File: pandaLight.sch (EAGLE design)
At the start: 158 parts, among them J1 PJ-037A, U1 MIC23451AAAYFL, U10 MT41J64M16, U11 PMOD-2X6, U12 PMOD-2X6, U13 PLR135-T10, U14 PLT133-T10W, U15 PLR135-T10, U16 TP10SQ, U17 TP10SQ, U18 PAN1322, U2 6SLX45CSG324, U3 TPD4S014SON, U4 FT2232HL, U5 93LC46BT-I/OT, U6 TPD12S016PWR, U7 TPD12S016PWR, U8 N25Q128AF8, U9 TPD12S016PWR, X1 USBUB-S, X2 HDMI_RECEPTICAL_A, X3 HDMI_RECEPTICAL_A, X4 HDMI_RECEPTICAL_A, Y1 403, Y2 20Mhz

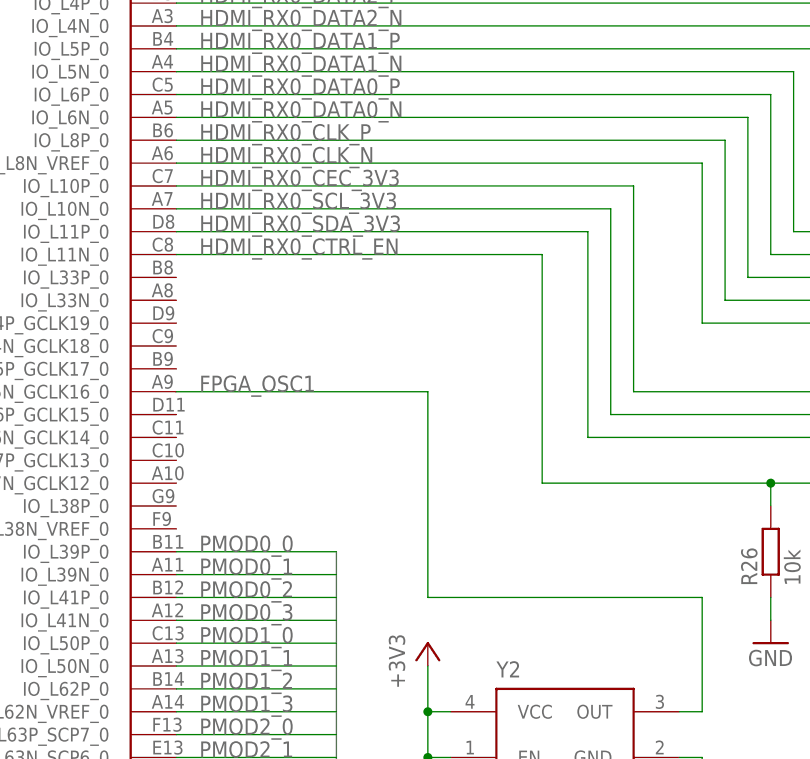
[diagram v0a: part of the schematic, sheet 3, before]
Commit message: Changed project name and file names to "pandaLight"; Routed connections FPGA to oscillator and HDMI_RX0
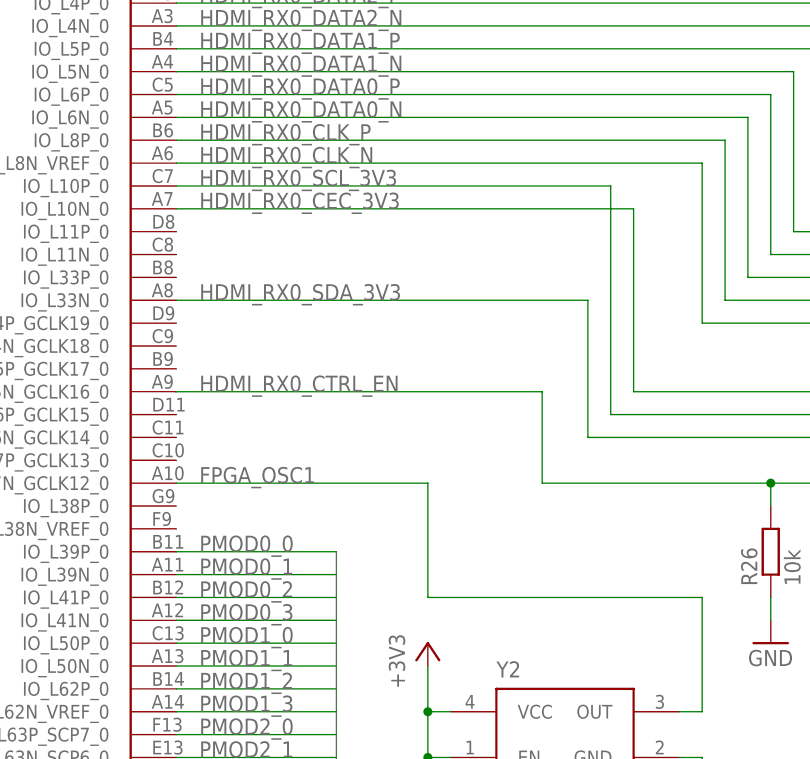
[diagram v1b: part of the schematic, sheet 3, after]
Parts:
- C1, C10, C2, C32, C6: device prj-hdmi:CAPACITOR1206 -> pandaLight:CAPACITOR1206
- C11, C12, C13, C14, C15, C16, C17, C18, C19, C20, C21, C22, C23, C24, C25, C26, C27, C28, C29, C3, C30, C31, C33, C34, C35, C36, C37, C38, C39, C4, C40, C41, C42, C43, C44, C45, C46, C47, C48, C49, C5, C50, C51, C52, C53, C54, C55, C56, C57, C58, C59, C60, C61, C62, C63, C64, C65, C66, C67, C68, C69, C7, C70, C8, C9: device prj-hdmi:CAPACITOR0402 -> pandaLight:CAPACITOR0402
- FB1, FB2: device prj-hdmi:FERRITE0402 -> pandaLight:FERRITE0402
- J1: device prj-hdmi:PJ-037A -> pandaLight:PJ-037A
- JP1, JP2, JP3: device prj-hdmi:JP2E -> pandaLight:JP2E
- L1, L2, L3: device prj-hdmi:INDUCTOR1008 -> pandaLight:INDUCTOR1008
- L4, L5: device prj-hdmi:INDUCTOR0603 -> pandaLight:INDUCTOR0603
- LED1, LED2: device prj-hdmi:LED0603 -> pandaLight:LED0603
- R1, R10, R11, R12, R13, R14, R15, R16, R17, R18, R19, R2, R20, R21, R22, R23, R24, R25, R26, R27, R28, R29, R3, R30, R31, R32, R33, R34, R35, R36, R37, R38, R39, R4, R40, R41, R42, R43, R44, R45, R46, R47, R5, R6, R7, R8, R9: device prj-hdmi:RESISTOR0402 -> pandaLight:RESISTOR0402
- RN1, RN2: device prj-hdmi:MNR18 -> pandaLight:MNR18
- SV1: device prj-hdmi:MA02-1 -> pandaLight:MA02-1
- SV2: device prj-hdmi:MA06-1 -> pandaLight:MA06-1
- U1: device prj-hdmi:MIC23451AAAYFL -> pandaLight:MIC23451AAAYFL
- U10: device prj-hdmi:MT41J64M16 -> pandaLight:MT41J64M16
- U11, U12: device prj-hdmi:PMOD-2X6 -> pandaLight:PMOD-2X6
- U13, U15: device prj-hdmi:PLR135-T10 -> pandaLight:PLR135-T10
- U14: device prj-hdmi:PLT133-T10W -> pandaLight:PLT133-T10W
- U16, U17: device prj-hdmi:TP10SQ -> pandaLight:TP10SQ
- U18: device prj-hdmi:PAN1322 -> pandaLight:PAN1322
- U2: device prj-hdmi:6SLX45CSG324 -> pandaLight:6SLX45CSG324
- U3: device prj-hdmi:TPD4S014SON -> pandaLight:TPD4S014SON
- U4: device prj-hdmi:FT2232HL -> pandaLight:FT2232HL
- U5: device prj-hdmi:93LC46BT-I/OT -> pandaLight:93LC46BT-I/OT
- U6, U7, U9: device prj-hdmi:TPD12S016PWR -> pandaLight:TPD12S016PWR
- U8: device prj-hdmi:N25Q128AF8 -> pandaLight:N25Q128AF8
- X1: device prj-hdmi:USBUB-S -> pandaLight:USBUB-S
- X2, X3, X4: device prj-hdmi:HDMI_RECEPTICAL_A -> pandaLight:HDMI_RECEPTICAL_A
- Y1: device prj-hdmi:403 -> pandaLight:403
- Y2: device prj-hdmi:636 -> pandaLight:636
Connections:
- net FPGA_OSC1: now also U2B0.IO_L37N_GCLK12_0; no longer U2B0.IO_L35N_GCLK16_0
- net HDMI_RX0_CEC_3V3: now also U2B0.IO_L10N_0; no longer U2B0.IO_L10P_0
- net HDMI_RX0_CTRL_EN: now also U2B0.IO_L35N_GCLK16_0; no longer U2B0.IO_L11N_0
- net HDMI_RX0_SCL_3V3: now also U2B0.IO_L10P_0; no longer U2B0.IO_L10N_0
- net HDMI_RX0_SDA_3V3: now also U2B0.IO_L33N_0; no longer U2B0.IO_L11P_0

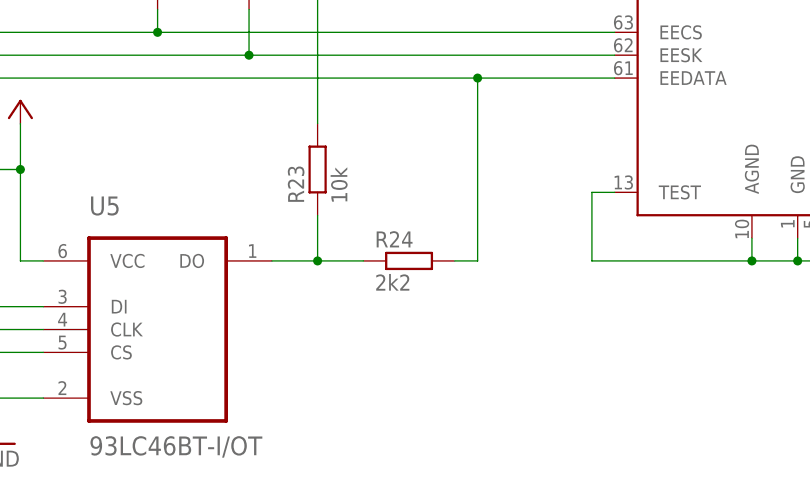
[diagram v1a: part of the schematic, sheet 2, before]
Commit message: Began adding BOM-ex parts
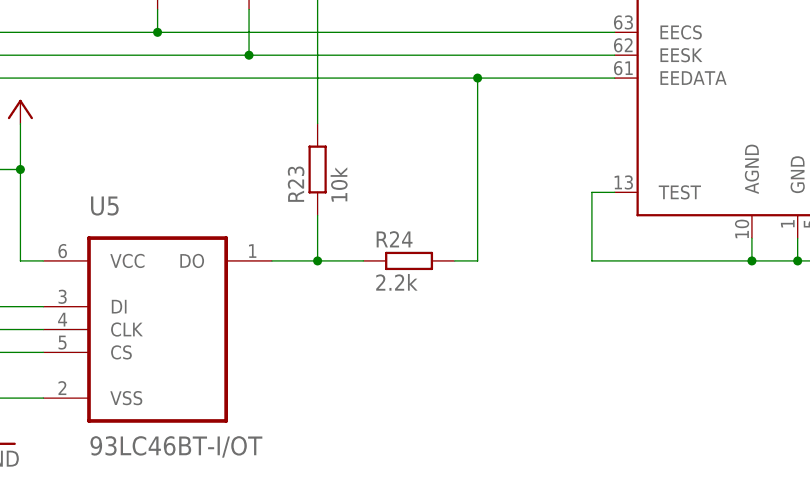
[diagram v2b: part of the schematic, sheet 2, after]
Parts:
- C1, C10, C2, C32, C6: PARTNO (none) -> CL31A107MQHNNNE
- C11, C15, C16, C17, C18, C23, C27, C29, C3, C31, C36, C43, C49, C55: PARTNO (none) -> C0603C475K9PACTU
- C12, C13, C14, C37, C38, C4, C44, C45, C5, C50, C51, C56, C57: PARTNO (none) -> C1005X5R0J474K050BB
- C19, C20, C21, C22, C24, C25, C26, C28, C30, C35, C39, C40, C41, C42, C46, C47, C48, C52, C53, C54, C60, C61, C62, C63, C64, C65, C66, C67, C68, C69, C70: PARTNO (none) -> CL05B104KP5NNNC
- C33, C34: PARTNO (none) -> CL05C270JB5NNNC
- C58, C59: PARTNO (none) -> C1005X5R0J105M050BB
- C7, C8, C9: device pandaLight:CAPACITOR0402 -> pandaLight:CAPACITOR0603; PARTNO (none) -> CL10A106MQ8NNNC
- FB1, FB2: PARTNO (none) -> BK1005HS100-T
- J1, JP1, JP2, JP3, LED2, SV1, SV2, U10, U11, U12, U13, U14, U15, U16, U17, U18, U3, U6, U7, U8, U9, X1: PARTNO (none) -> *
- L1, L2, L3: PARTNO (none) -> CIG22E1R0MNE
- L4, L5: PARTNO (none) -> GLFR1608T470M-LR
- LED1: PARTNO (none) -> LG Q971-KN-1
- R1, R16, R25, R27, R29, R34, R44, R45: PARTNO (none) -> ERJ-2RKF1001X
- R10, R12, R14, R15, R17, R18, R20, R21, R22, R23, R26, R28, R31, R33, R37, R46, R47, R5, R6, R8: PARTNO (none) -> ERJ-2RKF1002X
- R11: PARTNO (none) -> ERJ-2RKF2743X
- R13: PARTNO (none) -> ERJ-2RKF2943X
- R19: PARTNO (none) -> ERJ-2RKF1202X
- R2, R32, R36, R43: PARTNO (none) -> ERJ-2GEJ101X
- R24: value 2k2 -> 2.2k; PARTNO (none) -> ERJ-2RKF2201X
- R3: PARTNO (none) -> ERJ-2RKF3093X
- R30: PARTNO (none) -> ERJ-2RKF2401X
- R35, R38, R40, R41: PARTNO (none) -> ERJ-2RKF4701X
- R39: PARTNO (none) -> ERJ-2RKF1200X
- R4: PARTNO (none) -> ERJ-2RKF7152X
- R42: PARTNO (none) -> ERJ-2RKF2400X
- R7: PARTNO (none) -> ERJ-2RKF3163X
- R9: PARTNO (none) -> ERJ-2RKF2213X
- RN1, RN2: PARTNO (none) -> MNR18ERAPJ510
- U1: PARTNO (none) -> MIC23451-AAAYFL T5
- U2: PARTNO (none) -> XC6SLX45-3CSG324C
- U4: PARTNO (none) -> FT2232HL-REEL
- U5: PARTNO (none) -> 93LC46BT-I/OT
- X2, X3, X4: PARTNO (none) -> 10029449-111RLF
- Y1: PARTNO (none) -> 403C35D12M00000
- Y2: PARTNO (none) -> 636L3C020M00000

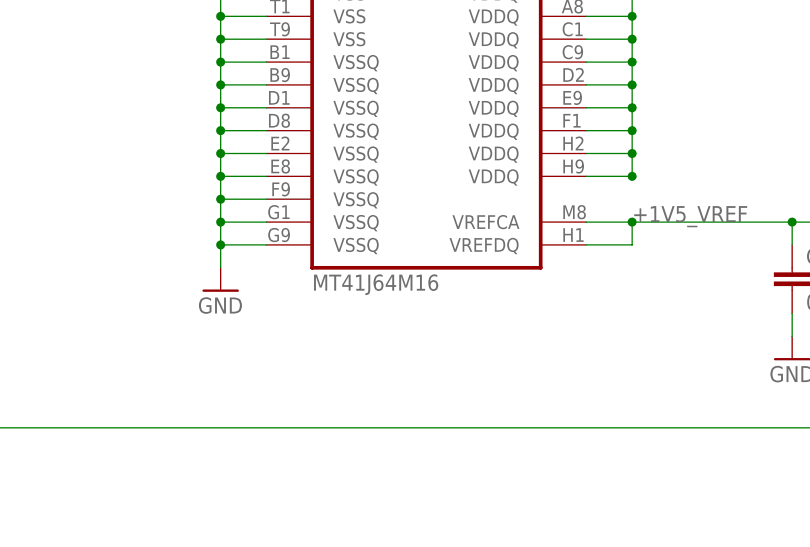
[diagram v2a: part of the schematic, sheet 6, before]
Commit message: Switched to an available DDR3 SDRAM chip; Finished first BOM-ex; Matched the length of the HDMI RX0 traces
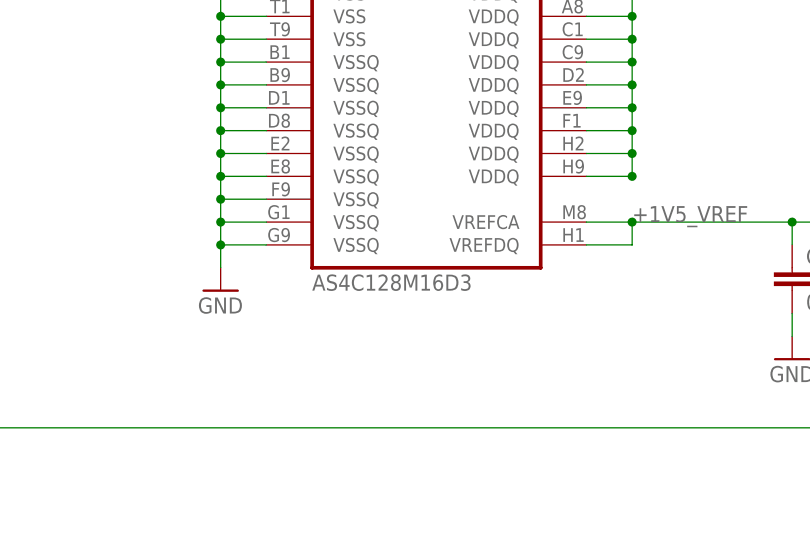
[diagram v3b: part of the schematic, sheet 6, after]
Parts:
- J1: PARTNO * -> PJ-037A
- LED2: PARTNO * -> LY Q976-P1S2-36
- U10: value MT41J64M16 -> AS4C128M16D3; device pandaLight:MT41J64M16 -> pandaLight:AS4C128M16D3; PARTNO * -> AS4C128M16D3-12BCN
- U11, U12: PARTNO * -> PPTC062LJBN-RC
- U13, U15: PARTNO * -> PLR135/T10
- U14: PARTNO * -> PLT133/T10W
- U16, U17: BOM (none) -> EXCLUDE
- U18: PARTNO * -> ENW-89841A3KF
- U3: PARTNO * -> TPD4S014DSQR
- U6, U7, U9: PARTNO * -> TPD12S016PWR
- U8: PARTNO * -> N25Q128A13EF840E
- X1: PARTNO * -> 10118192-0001LF
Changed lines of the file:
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@@
 <?xml version="1.0" encoding="utf-8"?>
 <!DOCTYPE eagle SYSTEM "eagle.dtd">
-<eagle version="6.5.0">
+<eagle version="6.6.0">
 <drawing>
 <settings>
@@
 <attribute name="PARTNO" value="XC6SLX45-3CSG324C"/>
 </part>
-<part name="U10" library="pandaLight" deviceset="MT41J64M16" device="">
-<attribute name="PARTNO" value="*"/>
+<part name="U10" library="pandaLight" deviceset="AS4C128M16D3" device="">
+<attribute name="PARTNO" value="AS4C128M16D3-12BCN"/>
 </part>
 <part name="GND52" library="pandaLight" deviceset="GND" device=""/>
@@
 </part>
 <part name="U6" library="pandaLight" deviceset="TPD12S016" device="PWR" value="TPD12S016PWR">
-<attribute name="PARTNO" value="*"/>
+<attribute name="PARTNO" value="TPD12S016PWR"/>
 </part>
 <part name="PS25" library="pandaLight" deviceset="+5V" device=""/>
@@
 <part name="GND35" library="pandaLight" deviceset="GND" device=""/>
 <part name="U7" library="pandaLight" deviceset="TPD12S016" device="PWR" value="TPD12S016PWR">
-<attribute name="PARTNO" value="*"/>
+<attribute name="PARTNO" value="TPD12S016PWR"/>
 </part>
 <part name="PS30" library="pandaLight" deviceset="+5V" device=""/>
@@
 <part name="GND43" library="pandaLight" deviceset="GND" device=""/>
 <part name="U9" library="pandaLight" deviceset="TPD12S016" device="PWR" value="TPD12S016PWR">
-<attribute name="PARTNO" value="*"/>
+<attribute name="PARTNO" value="TPD12S016PWR"/>
 </part>
 <part name="PS36" library="pandaLight" deviceset="+5V" device=""/>
@@
 </part>
 <part name="X1" library="pandaLight" deviceset="USB" device="UB-S" value="USBUB-S">
-<attribute name="PARTNO" value="*"/>
+<attribute name="PARTNO" value="10118192-0001LF"/>
 </part>
 <part name="GND25" library="pandaLight" deviceset="GND" device=""/>
@@
 </part>
 <part name="LED2" library="pandaLight" deviceset="LED" device="0603" value="Yellow">
-<attribute name="PARTNO" value="*"/>
+<attribute name="PARTNO" value="LY Q976-P1S2-36"/>
 </part>
 <part name="R38" library="pandaLight" deviceset="RESISTOR" device="0402" value="4.7k">
@@
 <part name="PS33" library="pandaLight" deviceset="+3V3" device=""/>
 <part name="U8" library="pandaLight" deviceset="N25Q128A" device="F8">
-<attribute name="PARTNO" value="*"/>
+<attribute name="PARTNO" value="N25Q128A13EF840E"/>
 </part>
 <part name="GND40" library="pandaLight" deviceset="GND" device=""/>
@@
 <part name="GND13" library="pandaLight" deviceset="GND" device=""/>
 <part name="U3" library="pandaLight" deviceset="TPD4S014" device="SON">
-<attribute name="PARTNO" value="*"/>
+<attribute name="PARTNO" value="TPD4S014DSQR"/>
 </part>
 <part name="GND18" library="pandaLight" deviceset="GND" device=""/>
@@
 </part>
 <part name="J1" library="pandaLight" deviceset="PJ-037A" device="">
-<attribute name="PARTNO" value="*"/>
+<attribute name="PARTNO" value="PJ-037A"/>
 </part>
 <part name="PS1" library="pandaLight" deviceset="+5V" device=""/>
@@
 </part>
 <part name="U11" library="pandaLight" deviceset="PMOD-2X6" device="">
-<attribute name="PARTNO" value="*"/>
+<attribute name="PARTNO" value="PPTC062LJBN-RC"/>
 </part>
 <part name="GND56" library="pandaLight" deviceset="GND" device=""/>
 <part name="GND57" library="pandaLight" deviceset="GND" device=""/>
 <part name="U12" library="pandaLight" deviceset="PMOD-2X6" device="">
-<attribute name="PARTNO" value="*"/>
+<attribute name="PARTNO" value="PPTC062LJBN-RC"/>
 </part>
 <part name="JP3" library="pandaLight" deviceset="JP2E" device="" value="PMOD2-3_VCC_SEL">
@@
 <part name="PS43" library="pandaLight" deviceset="+5V" device=""/>
 <part name="U14" library="pandaLight" deviceset="PLT133-T10W" device="">
-<attribute name="PARTNO" value="*"/>
+<attribute name="PARTNO" value="PLT133/T10W"/>
 </part>
 <part name="U15" library="pandaLight" deviceset="PLR135-T10" device="">
-<attribute name="PARTNO" value="*"/>
+<attribute name="PARTNO" value="PLR135/T10"/>
 </part>
 <part name="U13" library="pandaLight" deviceset="PLR135-T10" device="">
-<attribute name="PARTNO" value="*"/>
+<attribute name="PARTNO" value="PLR135/T10"/>
 </part>
 <part name="GND62" library="pandaLight" deviceset="GND" device=""/>
@@
 </part>
 <part name="U18" library="pandaLight" deviceset="PAN1322" device="">
-<attribute name="PARTNO" value="*"/>
+<attribute name="PARTNO" value="ENW-89841A3KF"/>
 </part>
 <part name="PS50" library="pandaLight" deviceset="+3V3" device=""/>
@@
 <part name="GND24" library="pandaLight" deviceset="GND" device=""/>
 <part name="U16" library="pandaLight" deviceset="TP" device="10SQ">
+<attribute name="BOM" value="EXCLUDE"/>
 <attribute name="PARTNO" value="*"/>
 </part>
 <part name="U17" library="pandaLight" deviceset="TP" device="10SQ">
+<attribute name="BOM" value="EXCLUDE"/>
 <attribute name="PARTNO" value="*"/>
 </part>
@@
 <instance part="U16" gate="G$1" x="10.16" y="66.04">
 <attribute name="PARTNO" x="10.16" y="66.04" size="1.778" layer="96" display="off"/>
+<attribute name="BOM" x="10.16" y="66.04" size="1.778" layer="96" rot="R90" display="off"/>
 </instance>
 <instance part="U17" gate="G$1" x="15.24" y="63.5">
 <attribute name="PARTNO" x="15.24" y="63.5" size="1.778" layer="96" display="off"/>
+<attribute name="BOM" x="15.24" y="63.5" size="1.778" layer="96" rot="R90" display="off"/>
 </instance>
 </instances>

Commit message: Switched the buck regulator to an available one; Corrected wrong packages and BOM-ex
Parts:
- removed U1: MIC23451AAAYFL, pandaLight:MIC23451AAAYFL
- added 1: MIC23450AAAYML, pandaLight:MIC23450AAAYML
- added C71, C72: 0.1u, pandaLight:CAPACITOR0402
- added R48, R49: 10k, pandaLight:RESISTOR0402
- C11, C18, C29, C3, C31: device pandaLight:CAPACITOR0402 -> pandaLight:CAPACITOR0603
- C15, C16, C17, C23, C27, C43, C49, C55: value 4.7u -> 0.1u; PARTNO C0603C475K9PACTU -> CL05B104KP5NNNC
- C19, C20, C25: value 0.1u -> 4.7u; device pandaLight:CAPACITOR0402 -> pandaLight:CAPACITOR0603; PARTNO CL05B104KP5NNNC -> C0603C475K9PACTU
- C32: value 100u -> 0.1u; device pandaLight:CAPACITOR1206 -> pandaLight:CAPACITOR0402; PARTNO CL31A107MQHNNNE -> CL05B104KP5NNNC
- C33: value 27p -> 4.7u; device pandaLight:CAPACITOR0402 -> pandaLight:CAPACITOR0603; PARTNO CL05C270JB5NNNC -> C0603C475K9PACTU
- C34: value 27p -> 100u; device pandaLight:CAPACITOR0402 -> pandaLight:CAPACITOR1206; PARTNO CL05C270JB5NNNC -> CL31A107MQHNNNE
- C35: value 0.1u -> 27p; PARTNO CL05B104KP5NNNC -> CL05C270JB5NNNC
- C36: value 4.7u -> 27p; PARTNO C0603C475K9PACTU -> CL05C270JB5NNNC
- C37, C44, C50, C56: value 0.47u -> 0.1u; PARTNO C1005X5R0J474K050BB -> CL05B104KP5NNNC
- C38, C45, C51, C57: value 0.47u -> 4.7u; device pandaLight:CAPACITOR0402 -> pandaLight:CAPACITOR0603; PARTNO C1005X5R0J474K050BB -> C0603C475K9PACTU
- C39, C40, C46, C47, C52, C53: value 0.1u -> 0.47u; PARTNO CL05B104KP5NNNC -> C1005X5R0J474K050BB
- C58, C59: value 1u -> 0.47u; PARTNO C1005X5R0J105M050BB -> C1005X5R0J474K050BB
- C60, C61: value 0.1u -> 1u; PARTNO CL05B104KP5NNNC -> C1005X5R0J105M050BB
- C7, C8, C9: value 10u -> 4.7u; PARTNO CL10A106MQ8NNNC -> C0603C475K9PACTU
- JP1, JP2, JP3, SV1, SV2: BOM (none) -> EXCLUDE
- R10, R12, R14, R8: value 10k -> 100k; PARTNO ERJ-2RKF1002X -> ERJ-2RKF1003X
- R11: value 274k -> 221k; PARTNO ERJ-2RKF2743X -> ERJ-2RKF2213X
- R13: value 294k -> 274k; PARTNO ERJ-2RKF2943X -> ERJ-2RKF2743X
- R15: value 10k -> 294k; PARTNO ERJ-2RKF1002X -> ERJ-2RKF2943X
- R16: value 1k -> 100k; PARTNO ERJ-2RKF1001X -> ERJ-2RKF1003X
- R18, R31, R46, R47: value 10k -> 1k; PARTNO ERJ-2RKF1002X -> ERJ-2RKF1001X
- R19: value 12k -> 10k; PARTNO ERJ-2RKF1202X -> ERJ-2RKF1002X
- R2: value 100 -> 51; PARTNO ERJ-2GEJ101X -> ERJ-2RKF51R0X
- R21: value 10k -> 12k; PARTNO ERJ-2RKF1002X -> ERJ-2RKF1202X
- R24: value 2.2k -> 10k; PARTNO ERJ-2RKF2201X -> ERJ-2RKF1002X
- R25: value 1k -> 10k; PARTNO ERJ-2RKF1001X -> ERJ-2RKF1002X
- R26: value 10k -> 2.2k; PARTNO ERJ-2RKF1002X -> ERJ-2RKF2201X
- R3: value 309k -> 51; PARTNO ERJ-2RKF3093X -> ERJ-2RKF51R0X
- R30: value 2.4k -> 10k; PARTNO ERJ-2RKF2401X -> ERJ-2RKF1002X
- R32: value 100 -> 2.4k; PARTNO ERJ-2GEJ101X -> ERJ-2RKF2401X
- R34, R45: value 1k -> 100; PARTNO ERJ-2RKF1001X -> ERJ-2GEJ101X
- R35: value 4.7k -> 10k; PARTNO ERJ-2RKF4701X -> ERJ-2RKF1002X
- R36: value 100 -> 1k; PARTNO ERJ-2GEJ101X -> ERJ-2RKF1001X
- R37: value 10k -> 4.7k; PARTNO ERJ-2RKF1002X -> ERJ-2RKF4701X
- R38: value 4.7k -> 100; PARTNO ERJ-2RKF4701X -> ERJ-2GEJ101X
- R39: value 120 -> 10k; PARTNO ERJ-2RKF1200X -> ERJ-2RKF1002X
- R4: value 71.5k -> 51; PARTNO ERJ-2RKF7152X -> ERJ-2RKF51R0X
- R41: value 4.7k -> 120; PARTNO ERJ-2RKF4701X -> ERJ-2RKF1200X
- R42: value 240 -> 4.7k; PARTNO ERJ-2RKF2400X -> ERJ-2RKF4701X
- R43: value 100 -> 4.7k; PARTNO ERJ-2GEJ101X -> ERJ-2RKF4701X
- R44: value 1k -> 240; PARTNO ERJ-2RKF1001X -> ERJ-2RKF2400X
- R5: value 10k -> 309k; PARTNO ERJ-2RKF1002X -> ERJ-2RKF3093X
- R6: value 10k -> 71.5k; PARTNO ERJ-2RKF1002X -> ERJ-2RKF7152X
- R7: value 316k -> 100k; PARTNO ERJ-2RKF3163X -> ERJ-2RKF1003X
- R9: value 221k -> 316k; PARTNO ERJ-2RKF2213X -> ERJ-2RKF3163X
- renumbered U10 to 10, U11 to 11, U12 to 12, U13 to 13, U14 to 14, U15 to 15, U16 to 16, U17 to 17, U18 to 18, U2 to 2, U3 to 3, U4 to 4, U5 to 5, U6 to 6, U7 to 7, U8 to 8, U9 to 9
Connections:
- new net N$30: 1.AVIN2, C16.1, R3.1
- new net N$48: 1.AVIN3, C15.1, R2.1
- net +1V2: now also 1.SNS3, C20.1, R13.2, R14.1; no longer C18.1, R11.2, R12.1, U1.SNS3
- net +1V5: now also 1.SNS2, C19.1, C63.1, C64.1, R10.1, R46.2, R9.2; no longer C17.1, C55.1, C56.1, R44.2, R7.2, R8.1, U1.SNS2
- net +1V5_VREF: now also C64.2, C66.1, C67.1, R46.1, R47.2; no longer C62.2, C63.1, C64.1, R44.1, R45.2
- net +1V8: now also C27.1, C28.1; no longer C23.1, C24.1
- net +3V3: now also 1.SNS1, C18.1, C23.1, C24.1, C33.1, C39.1, C40.1, C46.1, C47.1, C52.1, C53.1, C56.1, C71.1, C72.1, R16.1, R17.2, R20.1, R24.2, R27.2, R36.2, R37.2, R40.2, R48.2, R5.2, R7.1; no longer C15.1, C19.1, C20.1, C31.1, C35.1, C36.1, C41.1, C42.1, C48.1, C49.1, C54.1, C67.1, C70.1, R14.1, R15.2, R18.1, R20.2, R21.2, R3.2, R30.2, R31.2, R38.2, R46.2, R5.1, U1.SNS1
- net +5V: now also 1.PVIN1, 1.PVIN2, 1.PVIN3, C42.1, C49.1, C55.1, R12.1, R3.2, R4.2, R8.1; no longer C40.1, C47.1, C53.1, R10.1, R6.1, U1.PVIN1, U1.PVIN2, U1.PVIN3
- net BT_RESET#: now also R49.2; no longer R47.2
- net BT_WAKE: now also R48.1; no longer R46.1
- net DDR3_CK: now also R45.1; no longer R43.1
- net DDR3_CK#: now also R45.2; no longer R43.2
- net DDR3_CKE: now also R42.2; no longer R40.2
- net DDR3_RESET#: now also R43.2; no longer R41.2
- net GND: now also 1.AGND3, 1.ANGD1, 1.ANGD2, 1.EPAD, 1.PGND1, 1.PGND2, 1.PGND3, C62.2, C71.2, C72.2, R11.2, R15.2, R21.1, R30.1, R38.1, R39.1, R41.2, R43.1, R44.1, R49.1, R6.2; no longer C64.2, R13.2, R17.1, R26.1, R36.1, R37.1, R39.2, R4.2, R40.1, R41.1, R45.1, R9.2, U1.AGND@11, U1.ANGD@24, U1.EP1, U1.EP2, U1.PGND@1, U1.PGND@10, U1.PGND@2
- net HDMI_RX0_5V: now also C41.1, R29.1; no longer C39.1, R27.1
- net HDMI_RX0_CTRL_EN: now also R28.2; no longer R26.2
- net HDMI_RX1_5V: now also C48.1, R31.1; no longer C46.1, R29.1
- net HDMI_RX1_CTRL_EN: now also R30.2; no longer R28.2
- net HDMI_TX0_5V: now also C54.1; no longer C52.1
- net HDMI_TX0_CTRL_EN: now also R39.2; no longer R37.2
- net M3_RZQ: now also R41.1; no longer R39.1
- net N$1: now also C36.1; no longer C34.1
- net N$10: now also R26.2; no longer R24.2
- net N$11: now also R21.2; no longer R19.2
- net N$12: now also R25.1, R26.1; no longer R23.1, R24.1
- net N$13: now also R20.2; no longer R18.2
- net N$14: now also 1.SW1; no longer U1.SW1
- net N$15: now also 1.AVIN1, C17.1, R4.1; no longer C16.1, R2.1, U1.AVIN1, U1.AVIN2, U1.AVIN3
- net N$16: now also 1.SW2; no longer U1.SW2
- net N$17: now also 1.SW3; no longer U1.SW3
- net N$18: now also 1.FB3, R15.1; no longer R11.1, U1.FB3
- net N$20: now also 1.PG2, R10.2; no longer R8.2, U1.PG2
- net N$21: now also 1.FB1, R5.1, R6.1; no longer R3.1, R4.1, U1.FB1
- net N$22: now also 1.PG1, R7.2; no longer R5.2, U1.PG1
- net N$23: now also 1.FB2, R11.1; no longer R7.1, U1.FB2
- net N$24: now also 1.EN2, R12.2; no longer R10.2, U1.EN2
- net N$25: now also 1.EN1, R8.2; no longer R6.2, U1.EN1
- net N$26: now also 1.PG3, R14.2; no longer R12.2, U1.PG3
- net N$27: now also 1.EN3, R16.2; no longer R14.2, U1.EN3
- net N$28: now also C31.1, C32.1; no longer C29.1, C30.1
- net N$3: now also R44.2; no longer R42.2
- net N$31: now also C29.1, C30.1; no longer C27.1, C28.1
- net N$34: now also R37.1; no longer R35.1
- net N$35: now also R27.1; no longer R25.1
- net N$36: now also C68.1; no longer C66.1
- net N$37: now also R31.2; no longer R29.2
- net N$38: now also R36.1; no longer R34.1
- net N$39: now also R40.1; no longer R38.1
- net N$4: now also C70.1; no longer C68.1
- net N$41: now also R32.1; no longer R30.1
- net N$42: now also R34.1, R38.2; no longer R32.1, R36.2
- net N$44: now also R35.1; no longer R33.1
- net N$45: now also C34.1; no longer C32.1
- net N$46: now also R33.1; no longer R31.1
- net N$5: now also C35.1; no longer C33.1
- net N$50: now also R29.2; no longer R27.2
- net N$6: now also R22.1; no longer R20.1
- net N$9: now also R23.1; no longer R21.1
- net USB_5V_ACK#: now also R17.1, R18.1; no longer R15.1, R16.1
- net USB_5V_DISABLE: now also R19.2; no longer R17.2
- net USB_5V_OFF: now also R18.2; no longer R16.2
- net USB_PWRSAVE#: now also R24.1; no longer R22.1
